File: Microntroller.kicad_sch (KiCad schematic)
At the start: 12 parts, among them J3 Conn_01x02_Socket, SW2 SW_Push, U3 MCP1501-33xCH, U4 STM32C031C6T6, Y2 ABM8-48.000MHZ-B2-T

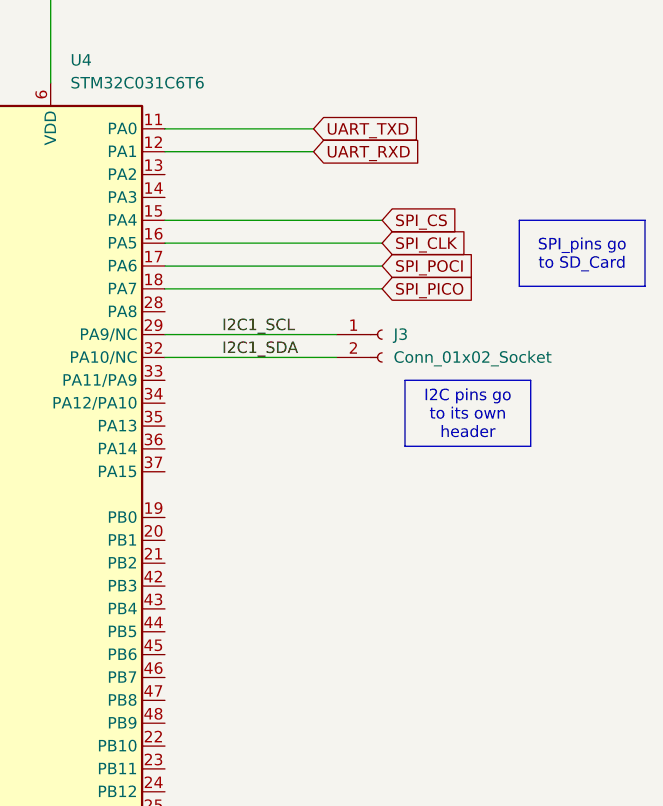
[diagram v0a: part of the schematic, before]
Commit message: updated schematics added the stm cube project file
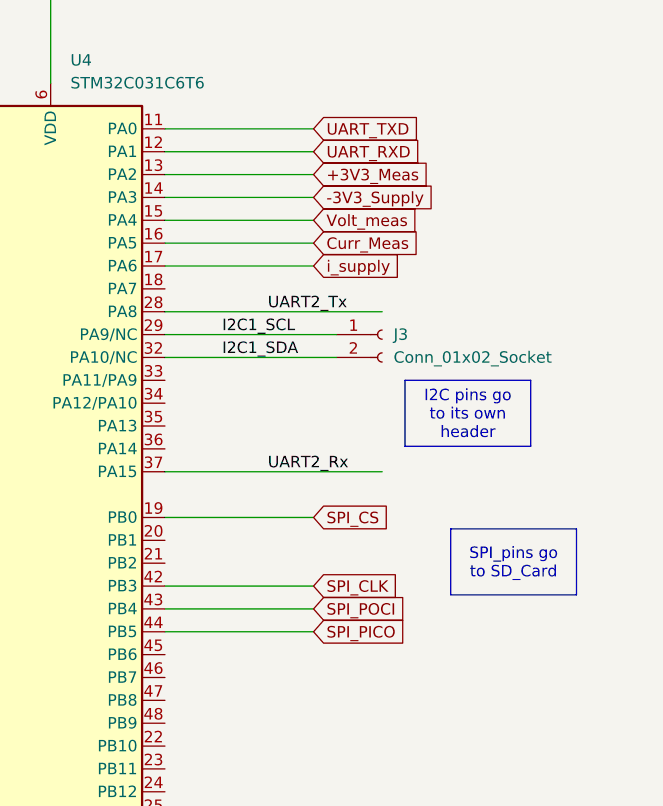
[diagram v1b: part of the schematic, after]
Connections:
- net SPI_CLK: now also U4.42 (PB3); no longer U4.16 (PA5)
- net SPI_CS: now also U4.19 (PB0); no longer U4.15 (PA4)
- net SPI_PICO: now also U4.44 (PB5); no longer U4.18 (PA7)
- net SPI_POCI: now also U4.43 (PB4); no longer U4.17 (PA6)
- net +3V3_Meas: now reaches U4.13 (PA2)
- net -3V3_Supply: now reaches U4.14 (PA3)
- net UART2_Tx: now reaches U4.28 (PA8)
- net UART2_Rx: now reaches U4.37 (PA15)
- new net Curr_Meas: U4.16 (PA5)
- new net Volt_meas: U4.15 (PA4)
- new net i_supply: U4.17 (PA6)
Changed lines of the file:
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@@
+	(wire
+		(pts
+			(xy 226.06 67.31) (xy 242.57 67.31)
+		)
+		(stroke
+			(width 0)
+			(type default)
+		)
+	)
 	(wire
 		(pts
@@
 	(wire
 		(pts
+			(xy 226.06 62.23) (xy 242.57 62.23)
+		)
+		(stroke
+			(width 0)
+			(type default)
+		)
+	)
+	(wire
+		(pts
 			(xy 69.85 50.8) (xy 198.12 50.8)
 		)
@@
 	(wire
 		(pts
-			(xy 226.06 62.23) (xy 250.19 62.23)
-		)
-		(stroke
-			(width 0)
-			(type default)
-		)
-	)
-	(wire
-		(pts
 			(xy 195.58 33.02) (xy 195.58 35.56)
 		)
@@
 	(wire
 		(pts
+			(xy 226.06 107.95) (xy 242.57 107.95)
+		)
+		(stroke
+			(width 0)
+			(type default)
+		)
+	)
+	(wire
+		(pts
 			(xy 226.06 74.93) (xy 245.11 74.93)
 		)
@@
 	(wire
 		(pts
+			(xy 226.06 102.87) (xy 242.57 102.87)
+		)
+		(stroke
+			(width 0)
+			(type default)
+		)
+	)
+	(wire
+		(pts
 			(xy 180.34 33.02) (xy 180.34 35.56)
 		)
@@
 	(wire
 		(pts
-			(xy 226.06 69.85) (xy 250.19 69.85)
-		)
-		(stroke
-			(width 0)
-			(type default)
-		)
-	)
-	(wire
-		(pts
 			(xy 132.08 57.15) (xy 198.12 57.15)
 		)
@@
 	(wire
 		(pts
+			(xy 226.06 90.17) (xy 250.19 90.17)
+		)
+		(stroke
+			(width 0)
+			(type default)
+		)
+	)
+	(wire
+		(pts
 			(xy 129.54 118.11) (xy 151.13 118.11)
 		)
@@
 	(wire
 		(pts
+			(xy 226.06 72.39) (xy 250.19 72.39)
+		)
+		(stroke
+			(width 0)
+			(type default)
+		)
+	)
+	(wire
+		(pts
 			(xy 24.13 43.18) (xy 24.13 45.72)
 		)
@@
 	(wire
 		(pts
+			(xy 226.06 64.77) (xy 242.57 64.77)
+		)
+		(stroke
+			(width 0)
+			(type default)
+		)
+	)
+	(wire
+		(pts
 			(xy 129.54 135.89) (xy 129.54 138.43)
 		)
@@
 	(wire
 		(pts
+			(xy 226.06 105.41) (xy 242.57 105.41)
+		)
+		(stroke
+			(width 0)
+			(type default)
+		)
+	)
+	(wire
+		(pts
 			(xy 180.34 24.13) (xy 180.34 25.4)
 		)
@@
 	(wire
 		(pts
+			(xy 226.06 95.25) (xy 242.57 95.25)
+		)
+		(stroke
+			(width 0)
+			(type default)
+		)
+	)
+	(wire
+		(pts
 			(xy 100.33 87.63) (xy 109.22 87.63)
 		)
@@
 	(wire
 		(pts
-			(xy 226.06 64.77) (xy 250.19 64.77)
+			(xy 226.06 57.15) (xy 242.57 57.15)
 		)
 		(stroke
@@
 	(wire
 		(pts
-			(xy 226.06 67.31) (xy 250.19 67.31)
+			(xy 226.06 59.69) (xy 242.57 59.69)
 		)
 		(stroke
@@
 	(text_box "SPI_pins go to SD_Card\n"
 		(exclude_from_sim no)
-		(at 265.43 62.23 0)
+		(at 257.81 96.52 0)
 		(size 13.97 7.3271)
 		(stroke
@@
 		)
 	)
+	(label "UART2_Tx"
+		(at 237.49 72.39 0)
+		(fields_autoplaced yes)
+		(effects
+			(font
+				(size 1.27 1.27)
+			)
+			(justify left bottom)
+		)
+	)
 	(label "OSC_OUT"
 		(at 146.05 59.69 0)
@@
 		)
 	)
+	(label "UART2_Rx"
+		(at 237.49 90.17 0)
+		(fields_autoplaced yes)
+		(effects
+			(font
+				(size 1.27 1.27)
+			)
+			(justify left bottom)
+		)
+	)
 	(label "I2C1_SCL"
 		(at 232.41 74.93 0)
@@
 	(global_label "SPI_CS"
 		(shape input)
-		(at 250.19 62.23 0)
-		(fields_autoplaced yes)
-		(effects
-			(font
-				(size 1.27 1.27)
-			)
-			(justify left)
-		)
-		(property "Intersheetrefs" "${INTERSHEET_REFS}"
-			(at 259.7066 62.23 0)
+		(at 242.57 95.25 0)
+		(fields_autoplaced yes)
+		(effects
+			(font
+				(size 1.27 1.27)
+			)
+			(justify left)
+		)
+		(property "Intersheetrefs" "${INTERSHEET_REFS}"
+			(at 252.0866 95.25 0)
+			(effects
+				(font
+					(size 1.27 1.27)
+				)
+				(justify left)
+				(hide yes)
+			)
+		)
+	)
+	(global_label "i_supply"
+		(shape input)
+		(at 242.57 67.31 0)
+		(fields_autoplaced yes)
+		(effects
+			(font
+				(size 1.27 1.27)
+			)
+			(justify left)
+		)
+		(property "Intersheetrefs" "${INTERSHEET_REFS}"
+			(at 253.2355 67.31 0)
+			(effects
+				(font
+					(size 1.27 1.27)
+				)
+				(justify left)
+				(hide yes)
+			)
+		)
+	)
+	(global_label "SPI_PICO"
+		(shape input)
+		(at 242.57 107.95 0)
+		(fields_autoplaced yes)
+		(effects
+			(font
+				(size 1.27 1.27)
+			)
+			(justify left)
+		)
+		(property "Intersheetrefs" "${INTERSHEET_REFS}"
+			(at 254.0824 107.95 0)
+			(effects
+				(font
+					(size 1.27 1.27)
+				)
+				(justify left)
+				(hide yes)
+			)
+		)
+	)
+	(global_label "-3V3_Supply"
+		(shape input)
+		(at 242.57 59.69 0)
+		(fields_autoplaced yes)
+		(effects
+			(font
+				(size 1.27 1.27)
+			)
+			(justify left)
+		)
+		(property "Intersheetrefs" "${INTERSHEET_REFS}"
+			(at 257.8921 59.69 0)
+			(effects
+				(font
+					(size 1.27 1.27)
+				)
+				(justify left)
+				(hide yes)
+			)
+		)
+	)
+	(global_label "SPI_POCI"
+		(shape input)
+		(at 242.57 105.41 0)
+		(fields_autoplaced yes)
+		(effects
+			(font
+				(size 1.27 1.27)
+			)
+			(justify left)
+		)
+		(property "Intersheetrefs" "${INTERSHEET_REFS}"
+			(at 254.0824 105.41 0)
+			(effects
+				(font
+					(size 1.27 1.27)
+				)
+				(justify left)
+				(hide yes)
+			)
+		)
+	)
+	(global_label "Volt_meas"
+		(shape input)
+		(at 242.57 62.23 0)
+		(fields_autoplaced yes)
+		(effects
+			(font
+				(size 1.27 1.27)
+			)
+			(justify left)
+		)
+		(property "Intersheetrefs" "${INTERSHEET_REFS}"
+			(at 255.1103 62.23 0)
+			(effects
+				(font
+					(size 1.27 1.27)
+				)
+				(justify left)
+				(hide yes)
+			)
+		)
+	)
+	(global_label "SPI_CLK"
+		(shape input)
+		(at 242.57 102.87 0)
+		(fields_autoplaced yes)
+		(effects
+			(font
+				(size 1.27 1.27)
+			)
+			(justify left)
+		)
+		(property "Intersheetrefs" "${INTERSHEET_REFS}"
+			(at 253.1752 102.87 0)
+			(effects
+				(font
+					(size 1.27 1.27)
+				)
+				(justify left)
+				(hide yes)
+			)
+		)
+	)
+	(global_label "Curr_Meas"
+		(shape input)
+		(at 242.57 64.77 0)
+		(fields_autoplaced yes)
+		(effects
+			(font
+				(size 1.27 1.27)
+			)
+			(justify left)
+		)
+		(property "Intersheetrefs" "${INTERSHEET_REFS}"
+			(at 255.2313 64.77 0)
 			(effects
 				(font
@@
 		)
 	)
-	(global_label "SPI_PICO"
-		(shape input)
-		(at 250.19 69.85 0)
-		(fields_autoplaced yes)
-		(effects
-			(font
-				(size 1.27 1.27)
-			)
-			(justify left)
-		)
-		(property "Intersheetrefs" "${INTERSHEET_REFS}"
-			(at 261.7024 69.85 0)
-			(effects
-				(font
-					(size 1.27 1.27)
-				)
-				(justify left)
-				(hide yes)
-			)
-		)
-	)
-	(global_label "SPI_POCI"
-		(shape input)
-		(at 250.19 67.31 0)
-		(fields_autoplaced yes)
-		(effects
-			(font
-				(size 1.27 1.27)
-			)
-			(justify left)
-		)
-		(property "Intersheetrefs" "${INTERSHEET_REFS}"
-			(at 261.7024 67.31 0)
-			(effects
-				(font
-					(size 1.27 1.27)
-				)
-				(justify left)
-				(hide yes)
-			)
-		)
-	)
-	(global_label "SPI_CLK"
-		(shape input)
-		(at 250.19 64.77 0)
-		(fields_autoplaced yes)
-		(effects
-			(font
-				(size 1.27 1.27)
-			)
-			(justify left)
-		)
-		(property "Intersheetrefs" "${INTERSHEET_REFS}"
-			(at 260.7952 64.77 0)
-			(effects
-				(font
-					(size 1.27 1.27)
-				)
-				(justify left)
-				(hide yes)
-			)
-		)
-	)
 	(global_label "UART_TXD"
 		(shape input)
@@
 			(effects
 				(font
+					(size 1.27 1.27)
+				)
+				(justify left)
+				(hide yes)
+			)
+		)
+	)
+	(global_label "+3V3_Meas"
+		(shape input)
+		(at 242.57 57.15 0)
+		(fields_autoplaced yes)
+		(effects
+			(font
+				(size 1.27 1.27)
+			)
+			(justify left)
+		)
+		(property "Intersheetrefs" "${INTERSHEET_REFS}"
+			(at 256.3199 57.15 0)
+			(effects
+				(font

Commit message: changes to schematic and PCB
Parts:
- C10, C11, C12, C13, C14, C8, C9: footprint (none) -> Capacitor_SMD:C_0805_2012Metric
- J3: footprint (none) -> Connector_Molex:Molex_KK-254_AE-6410-02A_1x02_P2.54mm_Vertical
- SW2: footprint (none) -> Button_Switch_THT:SW_PUSH_6mm
- Y2: value ABM8-48.000MHZ-B2-T -> 16 MHz Crystal; footprint (none) -> Oscillator:Oscillator_SMD_Abracon_ASE-4Pin_3.2x2.5mm_HandSoldering
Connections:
- net PC13: now reaches U4.1 (PC13)
- net PA7: now reaches U4.18 (PA7)
- net PC14: now reaches U4.2 (PC14)
- net PB1: now reaches U4.20 (PB1)
- net PB2: now reaches U4.21 (PB2)
- net PB10: now reaches U4.22 (PB10)
- net PB11: now reaches U4.23 (PB11)
- net PB12: now reaches U4.24 (PB12)
- net PB13: now reaches U4.25 (PB13)
- net PB14: now reaches U4.26 (PB14)
- net PB15: now reaches U4.27 (PB15)
- net PC15: now reaches U4.3 (PC15)
- net PC6: now reaches U4.30 (PC6)
- net PC7: now reaches U4.31 (PC7)
- net PA11/PA9: now reaches U4.33 (PA11/PA9)
- net PA12/PA10: now reaches U4.34 (PA12/PA10)
- net PA13: now reaches U4.35 (PA13)
- net PA14: now reaches U4.36 (PA14)
- net PD0: now reaches U4.38 (PD0)
- net PD1: now reaches U4.39 (PD1)
- net PF3: now reaches U4.4 (PF3)
- net PD2: now reaches U4.40 (PD2)
- net PD3: now reaches U4.41 (PD3)
- net PB6: now reaches U4.45 (PB6)
- net PB7: now reaches U4.46 (PB7)
- net PB8: now reaches U4.47 (PB8)
- net PB9: now reaches U4.48 (PB9)
- net Curr_Meas renamed Curr_meas
- net SPI_CLK renamed SPI_Clk
- net SPI_CS renamed SPI_Cs
- net SPI_PICO renamed SPI_Mosi
- net SPI_POCI renamed SPI_Miso
- net UART_RXD renamed UART1_Rx
- net UART_TXD renamed UART1_Tx
- net i_supply renamed i_Supply
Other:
- moved on the sheet: C10, C8, U3

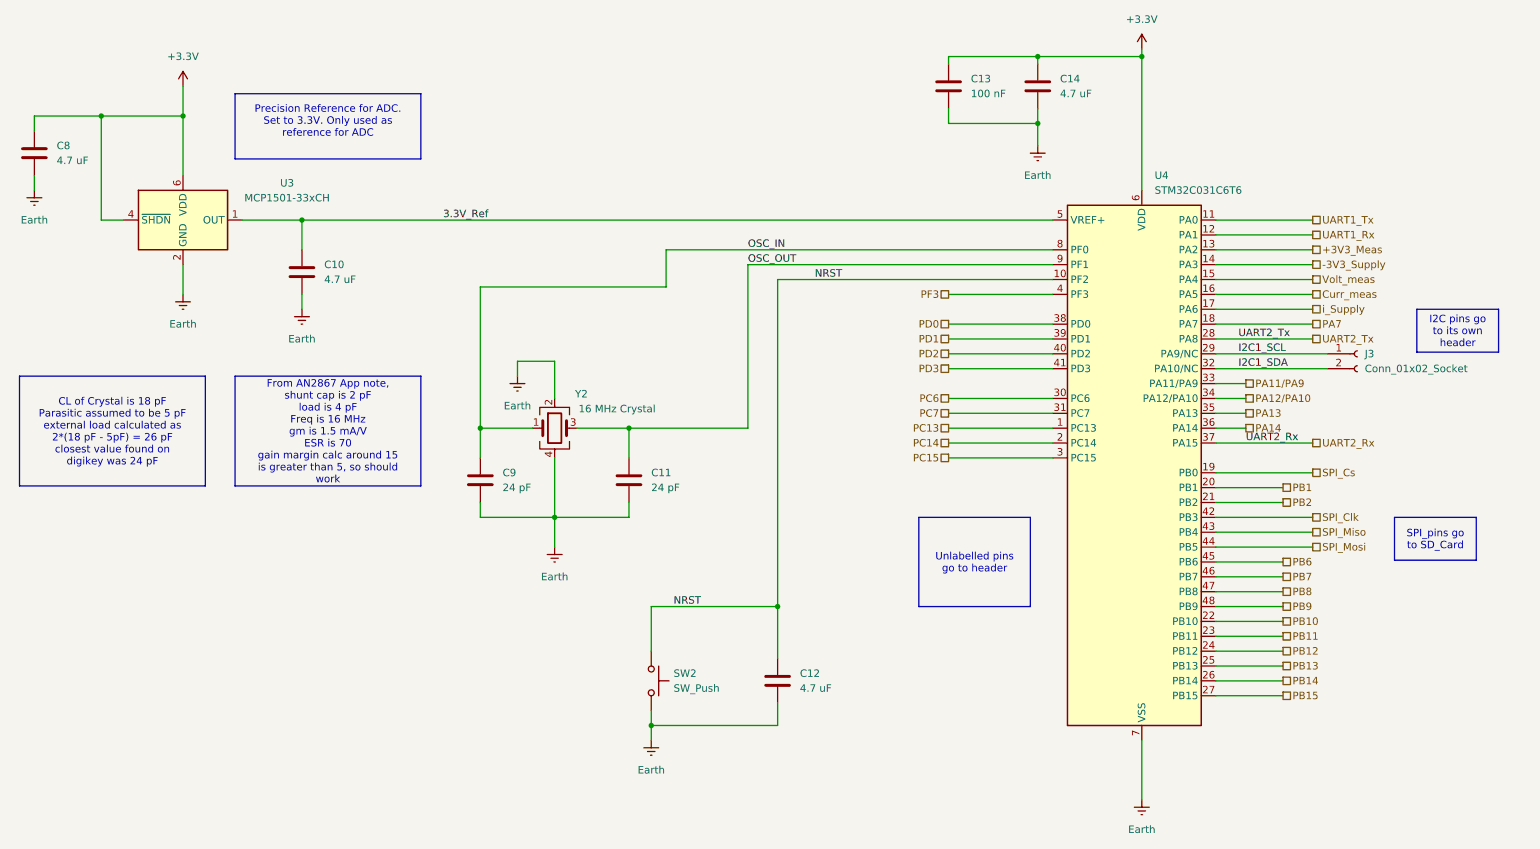
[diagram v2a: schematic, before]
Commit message: changed schematics
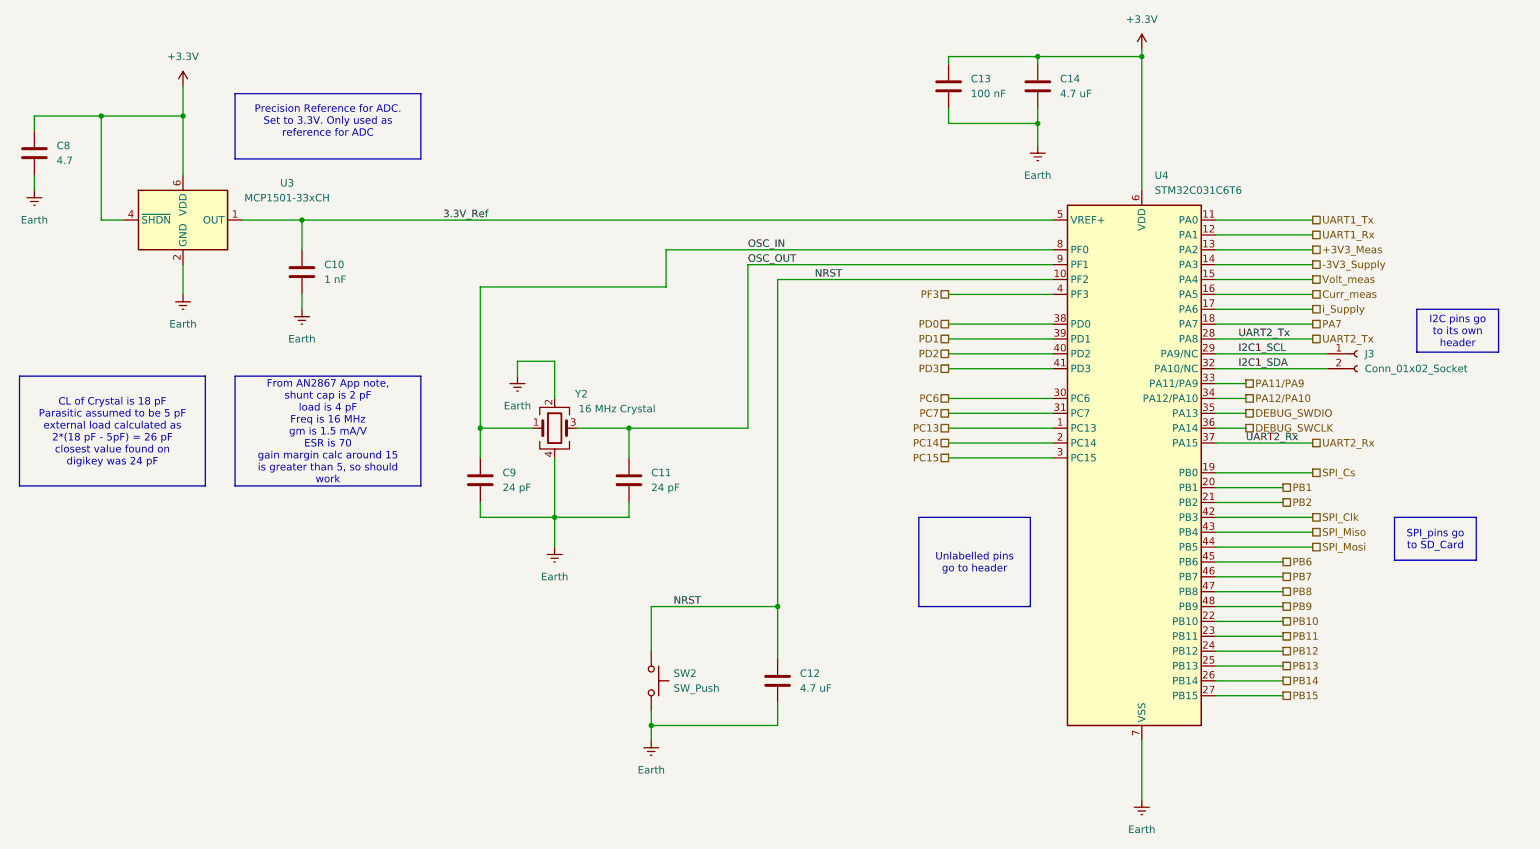
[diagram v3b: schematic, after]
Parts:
- C10: value 4.7 uF -> 1 nF
- C8: value 4.7 uF -> 4.7
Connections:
- net PA13 renamed DEBUG_SWDIO
- net PA14 renamed DEBUG_SWCLK
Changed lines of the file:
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@@
 		)
 	)
-	(hierarchical_label "PA14"
+	(hierarchical_label "DEBUG_SWCLK"
 		(shape passive)
 		(at 231.14 87.63 0)
@@
 		)
 	)
-	(hierarchical_label "PA13"
+	(hierarchical_label "DEBUG_SWDIO"
 		(shape passive)
 		(at 231.14 85.09 0)
@@
 			)
 		)
-		(property "Value" "4.7 uF"
+		(property "Value" "4.7"
 			(at 27.94 41.9099 0)
 			(effects
@@
 			)
 		)
-		(property "Value" "4.7 uF"
+		(property "Value" "1 nF"
 			(at 73.66 62.2299 0)
 			(effects
